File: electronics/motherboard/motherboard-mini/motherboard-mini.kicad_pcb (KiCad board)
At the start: 2 copper layers, 106.6 x 156.6 mm, 189 parts, among them J1 JTAG, J10 CONUFL001-SMD-T, J11 SIM8060-6-0-14-00-A, J12 JTAG, J2 ST1W008S4AR1500, J3 2604-3102, J4 2604-3105, J5 USB4070-30-C_REVC5, J6 2604-3102, J7 SOLAR_CRNT_JMPR, J8 BAT_CRNT_JMPR, J9 2604-3102, Q1 MMDT3904, Q2 BC847, Q3 BSS214NW, Q4 BC847, Q5 BC847, Q6 BSS214NW, SW1 BOOT, SW2 RESET, SW4 CAT_M1_RST, U1 CP2102N-Axx-xQFN28, U10 TPS22967DSGR, U11 SARA-R410M-02B, U13 TXB0104PW, U14 TCA9534, U2 ESP32-WROOM-32E_(16MB), U3 INA219BxD, U4 LT3652IMSE, U5 MCP73832-2-OT, U6 INA219BxD, U7 MIC2288YD5-TR, U8 XC6215B332MR-G, U9 NCP718xSN500, Y1 32.768KHz

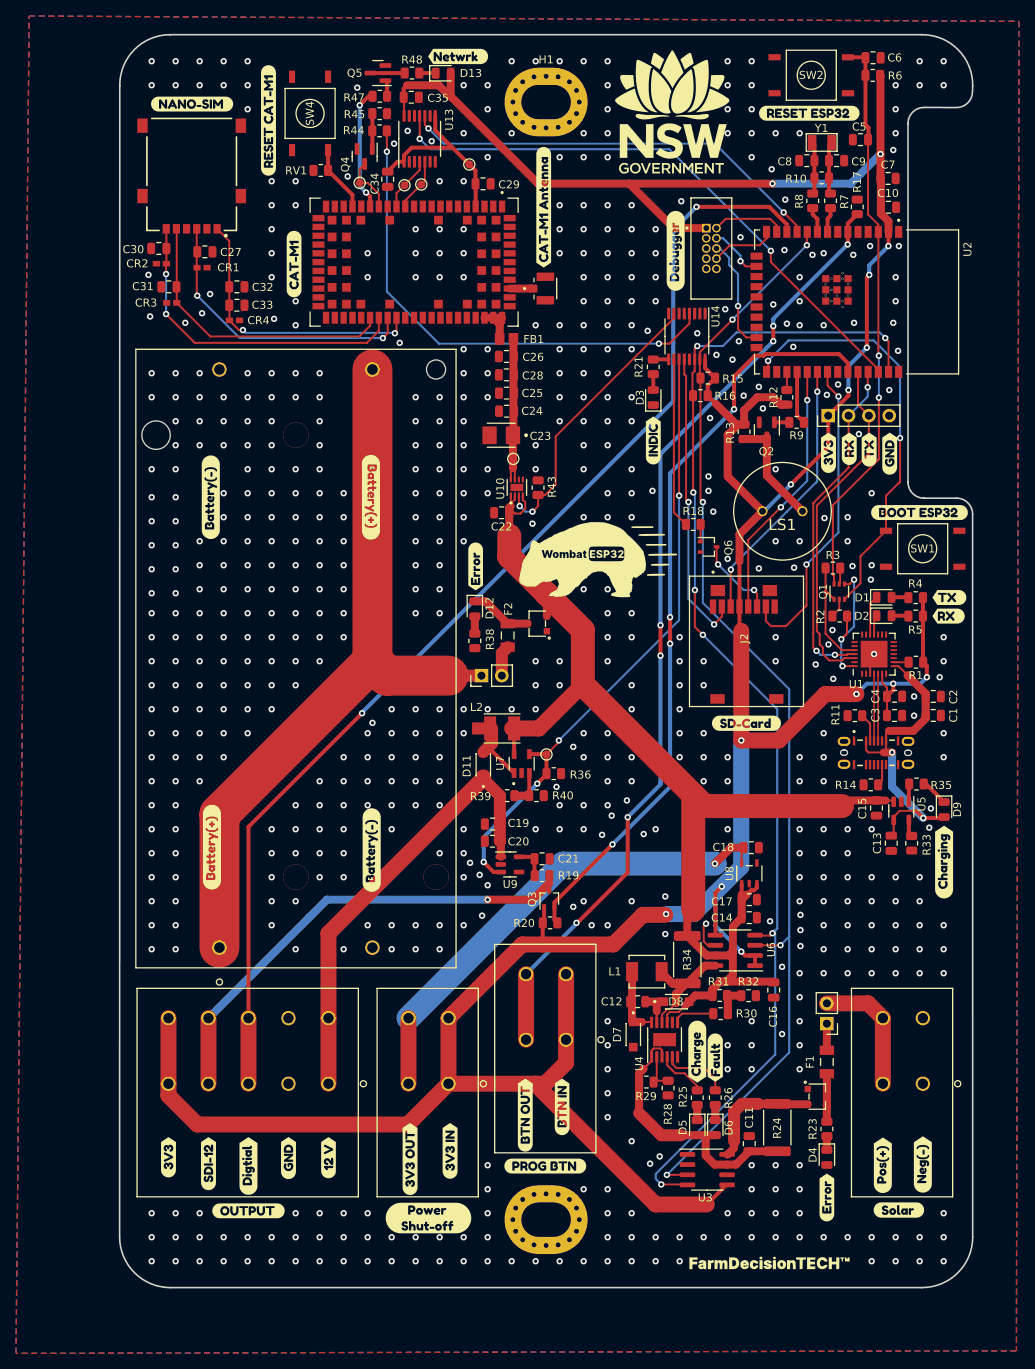
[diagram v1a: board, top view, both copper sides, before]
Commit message: new version sent for manufacture, updated component positioning, removed level shifter on SDI-12 line, re routed the solar charge circuit
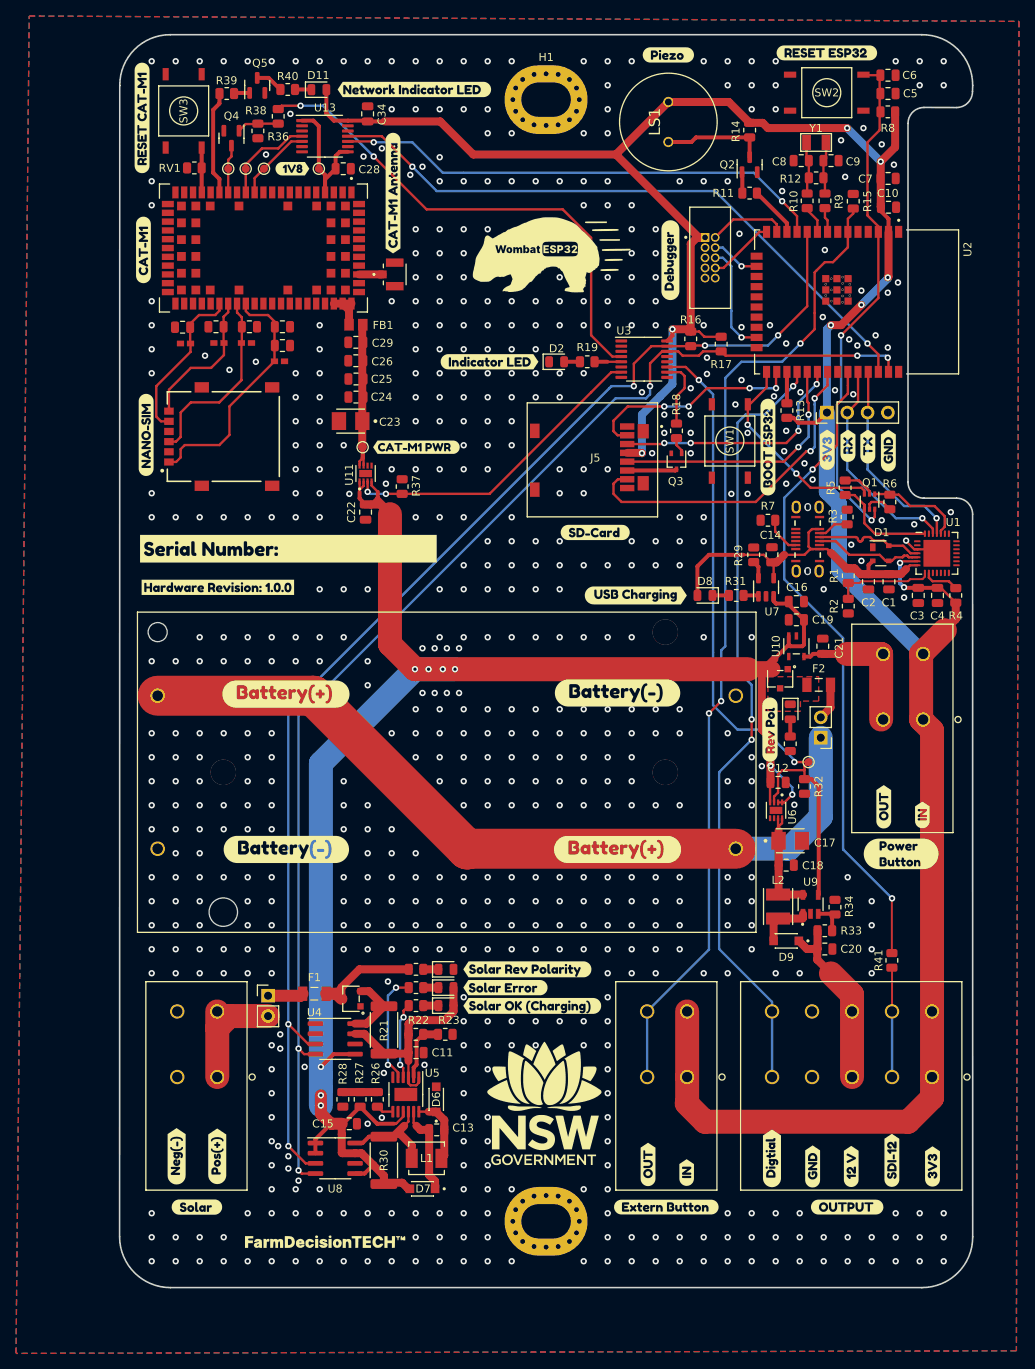
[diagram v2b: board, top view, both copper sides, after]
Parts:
- removed the C20 at (78.6, 127.5)
- removed the C21 at (84.8, 129.7)
- removed the C34 at (65.5, 44.8)
- removed the D2 at (127.5, 99.3)
- removed the Q3 at (85.7, 134.7)
- removed the R19 at (84.8, 131.8)
- removed the R20 at (85.8, 137.7)
- removed the R4 at (131.5, 97.0)
- removed the R5 at (131.5, 99.4)
- removed the U9 at (80.8, 130.4)
- removed kibuzzard-635F8E2B (x2): G***, kibuzzard-635F8E2B
- removed kibuzzard-635F8E59 (x2): G***, kibuzzard-635F8E59
- removed kibuzzard-635F91A1: G***, kibuzzard-635F91A1
- removed kibuzzard-635F91AE: G***, kibuzzard-635F91AE
- removed kibuzzard-6360A408: G***, kibuzzard-6360A408
- removed kibuzzard-63643555: G***, kibuzzard-63643555
- removed kibuzzard-636459CC: G***, kibuzzard-636459CC
- removed kibuzzard-6364640A: G***, kibuzzard-6364640A
- removed kibuzzard-63648775: G***, kibuzzard-63648775
- removed kibuzzard-637470B7: G***, kibuzzard-637470B7
- removed kibuzzard-637470C3: G***, kibuzzard-637470C3
- removed kibuzzard-63747569: G***, kibuzzard-63747569
- removed kibuzzard-63747865: G***, kibuzzard-63747865
- removed kibuzzard-63747876: G***, kibuzzard-63747876
- removed kibuzzard-637478F4: G***, kibuzzard-637478F4
- removed kibuzzard-6374797E: G***, kibuzzard-6374797E
- removed kibuzzard-6374798A: G***, kibuzzard-6374798A
- added C13: 1uF, Capacitor_SMD:C_0805_2012Metric, F.Cu at (71.6, 163.6)
- added C19: 1uF, Capacitor_SMD:C_0805_2012Metric, F.Cu at (116.6, 99.8)
- added R1: 22.1K, Resistor_SMD:R_0805_2012Metric, F.Cu at (123.1, 94.3)
- added R2: 47.5K, Resistor_SMD:R_0805_2012Metric, F.Cu at (123.1, 98.1)
- added R41: 0, Resistor_SMD:R_0805_2012Metric, F.Cu at (128.5, 142.4)
- added U6: TPS22967DSGR, TPS22967DSGR:SON50P200X200X80-9N, F.Cu at (114.0, 123.6)
- added kibuzzard-639304A2: G***, kibuzzard-639304A2, F.Cu at (113.3, 113.5)
- added kibuzzard-63932112: G***, kibuzzard-63932112, F.Cu at (83.0, 143.5)
- added kibuzzard-639322B3: G***, kibuzzard-639322B3, F.Cu at (44.3, 95.8)
- added kibuzzard-63932346: G***, kibuzzard-63932346, F.Cu at (129.7, 129.1)
- added kibuzzard-63932369: G***, kibuzzard-63932369, F.Cu at (96.5, 96.8)
- added kibuzzard-63969873: G***, kibuzzard-63969873, F.Cu at (53.1, 90.9)
- added kibuzzard-6396A059: G***, kibuzzard-6396A059, F.Cu at (100.6, 29.2)
- added kibuzzard-6396A3EF: G***, kibuzzard-6396A3EF, F.Cu at (53.6, 43.4)
- added kibuzzard-6396A450: G***, kibuzzard-6396A450, F.Cu at (69.1, 78.2)
- added kibuzzard-6396A474: G***, kibuzzard-6396A474, F.Cu at (78.2, 67.6)
- added kibuzzard-6397AB25: G***, kibuzzard-6397AB25, F.Cu at (52.8, 128.5)
- added kibuzzard-6397AB25: G***, kibuzzard-6397AB25, F.Cu at (94.2, 109.0)
- added kibuzzard-6397AB35: G***, kibuzzard-6397AB35, F.Cu at (52.8, 109.1)
- added kibuzzard-6397AB35: G***, kibuzzard-6397AB35, F.Cu at (94.2, 128.5)
- added kibuzzard-6397BE2B: G***, kibuzzard-6397BE2B, F.Cu at (83.6, 148.1)
- added kibuzzard-6397BE4E: G***, kibuzzard-6397BE4E, F.Cu at (80.2, 145.8)
- added kibuzzard-639A4BB4: G***, kibuzzard-639A4BB4, F.Cu at (127.5, 123.2)
- added kibuzzard-639A4BB4: G***, kibuzzard-639A4BB4, F.Cu at (98.0, 167.9)
- added kibuzzard-639A4BC1: G***, kibuzzard-639A4BC1, F.Cu at (132.3, 124.2)
- added kibuzzard-639A4BC1: G***, kibuzzard-639A4BC1, F.Cu at (102.9, 168.9)
- added kibuzzard-639A4BEA: G***, kibuzzard-639A4BEA, F.Cu at (100.3, 173.2)
- added kibuzzard-639A4C0B: G***, kibuzzard-639A4C0B, F.Cu at (68.8, 33.5)
- C17: value 1uF -> 100uF; footprint Capacitor_SMD:C_0805_2012Metric -> T520B107M006ATE015:CAPPM3528X210N
- C21: renamed from C18; value 0.1 -> 0.1uF
- D1: value LED(Orange) -> SP0503BAHT; footprint LED_SMD:LED_0805_2012Metric -> Package_TO_SOT_SMD:SOT-143
- D11: renamed from D13; value LED -> LED(Orange)
- D2: renamed from D3; value LED(Yellow) -> LED(Orange)
- D8: renamed from D9; value LED -> LED(Green)
- J1: renamed from J5; value USB4070-30-C_REVC5 -> USB4145-03-0230-C
- R19: renamed from R21; value 1.2K -> 1K
- R35: renamed from R38; value 1.5K -> 1K
- R40: renamed from R48; value 1.2K -> 1K
- moved G*** 125.0 mm to (85.3, 160.6)
- moved kibuzzard-635F8A75 95.5 mm to (133.6, 168.1)
- moved kibuzzard-63606B62 93.3 mm to (39.1, 166.9)
- moved J7 88.2 mm to (44.2, 157.0)
- moved kibuzzard-63606B27 87.7 mm to (41.7, 173.2)
- moved kibuzzard-6374791F 85.4 mm to (128.5, 167.4)
- moved kibuzzard-63606B50 83.2 mm to (44.2, 166.9)
- moved J6 75.5 mm to (133.5, 157.0)
- moved kibuzzard-63747585 74.8 mm to (122.9, 173.2)
- moved J10 74.8 mm to (132.4, 112.3)
- moved J8 69.9 mm to (50.5, 146.8), turned to 0 degrees
- moved B1 65.7 mm to (109.0, 128.4), turned to 180 degrees
- moved kibuzzard-635F8A8D 65.5 mm to (118.6, 168.1)
- moved kibuzzard-63747928 65.4 mm to (113.5, 167.1)
- moved kibuzzard-63747933 65.4 mm to (123.4, 168.1)
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- renumbered C13 to C14, C14 to C15, C15 to C16, C16 to C18, C19 to C20, C28 to C26, C29 to C28, C26 to C29, C35 to C34, D12 to D10, D4 to D3, D5 to D4, D6 to D5, D7 to D6, D8 to D7, D11 to D9, J9 to J10, J10 to J11, J11 to J12, J1 to J2, J12 to J3, J3 to J4, J2 to J5, J4 to J6, J6 to J7, J7 to J8, J8 to J9, Q6 to Q3, R8 to R10, R9 to R11, R10 to R12, R12 to R13, R13 to R14, R17 to R15, R15 to R16, R16 to R17, R23 to R20, R24 to R21, R29 to R22, R28 to R23, R25 to R24, R26 to R25, R30 to R26, R31 to R27, R32 to R28, R33 to R29, R11 to R3, R34 to R30, R35 to R31, R36 to R32, R39 to R33, R40 to R34, R44 to R36, R43 to R37, R45 to R38, R47 to R39, R1 to R4, R2 to R5, R3 to R6, R14 to R7, R6 to R8, R7 to R9, SW4 to SW3, U8 to U10, U10 to U11, U11 to U12, U14 to U3, U3 to U4, U4 to U5, U5 to U7, U6 to U8, U7 to U9
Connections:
- net IO_P1 renamed IO_P6
- C12 pad 1: Net-(C12-Pad1) -> GND
- C12 pad 2: Net-(C12-Pad2) -> VBAT
- C17 pad 1: VBAT -> Net-(C17-Pad1)
- C18 pad 1: VBAT -> Net-(C17-Pad1)
- C22 pad 1: VBAT -> GND
- C22 pad 2: GND -> VBAT
- D1 pad 1: Net-(D1-Pad1) -> GND
- D1 pad 2: Net-(D1-Pad2) -> VBUS
- D6 pad C: Net-(C12-Pad1) -> Net-(C13-Pad2)
- D7 pad C: Net-(C12-Pad2) -> Net-(C13-Pad1)
- J2 pad 2: UART_RX0 -> UART_TX0
- J2 pad 3: UART_TX0 -> UART_RX0
- J5 pad 2: IO_P2 -> GPIO4
- J6 pad 1: +12V -> +3.3V
- J6 pad 10: +3.3V -> GPIO17
- J6 pad 2: +12V -> +3.3V
- J6 pad 3: GND -> GPIO21
- J6 pad 4: GND -> GPIO21
- J6 pad 5: GPIO27 -> +12V
- J6 pad 6: GPIO27 -> +12V
- J6 pad 7: SDI12_IN_OUT -> GND
- J6 pad 8: SDI12_IN_OUT -> GND
- J6 pad 9: +3.3V -> GPIO17
- J7 pad 1: GND -> Net-(J7-Pad1)
- J7 pad 2: GND -> Net-(J7-Pad1)
- J7 pad 3: Net-(J6-Pad4) -> GND
- J7 pad 4: Net-(J6-Pad4) -> GND
- J8 pad 2: Net-(J6-Pad4) -> Net-(J7-Pad1)
- L1 pad 1: Net-(C12-Pad1) -> Net-(C13-Pad2)
- L2 pad 1: VBAT -> Net-(C17-Pad1)
- R11 pad 1: GPIO17 -> GPIO27
- R19 pad 1: Net-(U14-Pad9) -> Net-(R19-Pad1)
- U1 pad 18: Net-(D2-Pad1) -> unconnected-(U1-Pad18)
- U1 pad 19: Net-(D1-Pad1) -> unconnected-(U1-Pad19)
- U1 pad 7: unconnected-(U1-Pad7) -> VBUS
- U1 pad 8: VBUS -> Net-(R1-Pad2)
- U2 pad 26: unconnected-(U2-Pad26) -> GPIO4
- U2 pad 33: GPIO21 -> Net-(U2-Pad33)
- U3 pad 12: IO_P2 -> unconnected-(U3-Pad12)
- U3 pad 5: unconnected-(U14-Pad5) -> Net-(R19-Pad1)
- U3 pad 9: Net-(U14-Pad9) -> unconnected-(U3-Pad9)
- U4 pad 5: +3.3V -> VBAT
- U5 pad 11: Net-(C12-Pad2) -> Net-(C13-Pad1)
- U5 pad 12: Net-(C12-Pad1) -> Net-(C13-Pad2)
- U8 pad 1: +3.3V -> VBAT
- U8 pad 2: +3.3V -> VBAT
- U8 pad 5: +3.3V -> VBAT
- U9 pad 5: VBAT -> Net-(C17-Pad1)
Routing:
- net GPIO27: track 145.9 -> 6.40 mm, vias 2 -> 0
- net +3.3V: track 453.5 -> 350.6 mm, vias 14 -> 9
- net GPIO17: track 6.66 -> 97.8 mm, vias 0 -> 3
- net Net-(U2-Pad33): track 0.00 -> 81.5 mm, vias 0 -> 2
- net GPIO21: track 94.7 -> 13.7 mm, vias 4 -> 0
- net VBAT: track 154.0 -> 229.9 mm, vias 0 -> 9
- net SDI12_IN_OUT: track 59.7 -> 0.00 mm, vias 1 -> 0
- net Net-(C21-Pad1): track 61.0 -> 18.0 mm, vias 1 -> 0
- net IO_P2: track 37.3 -> 0.00 mm, vias 2 -> 0
- net +12V: track 57.2 -> 22.8 mm
- net GPIO4: track 0.00 -> 27.3 mm, vias 0 -> 4
- net GPIO0: track 52.3 -> 26.2 mm
- net Net-(C30-Pad1): track 41.0 -> 18.0 mm, vias 2 -> 0
- net I2C_SDA: track 141.7 -> 159.9 mm
- net UART_RX0: track 42.8 -> 25.3 mm, vias 3 -> 1
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- added copper zone on F.Cu, net Net-(D10-Pad1)
